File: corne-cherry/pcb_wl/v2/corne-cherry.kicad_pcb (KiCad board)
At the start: 2 copper layers, 152.8 x 91.4 mm, 72 parts, among them J1 MJ-4PP-9, J2 OLED, J3 Conn_01x02_Female, SW1 SW_PUSH, SW10 SW_PUSH, SW11 SW_PUSH, SW12 SW_PUSH, SW13 SW_PUSH, SW14 SW_PUSH, SW15 SW_PUSH, SW16 SW_PUSH, SW17 SW_PUSH, SW18 SW_PUSH, SW19 SW_PUSH, SW2 SW_PUSH, SW20 SW_PUSH, SW21 SW_PUSH, SW22 SW_PUSH, SW23 SW_SPDT, SW24 SW_SPDT, SW3 SW_PUSH, SW4 SW_PUSH, SW5 SW_PUSH, SW6 SW_PUSH, SW7 SW_PUSH, SW8 SW_PUSH, SW9 SW_PUSH, U1 ProMicro

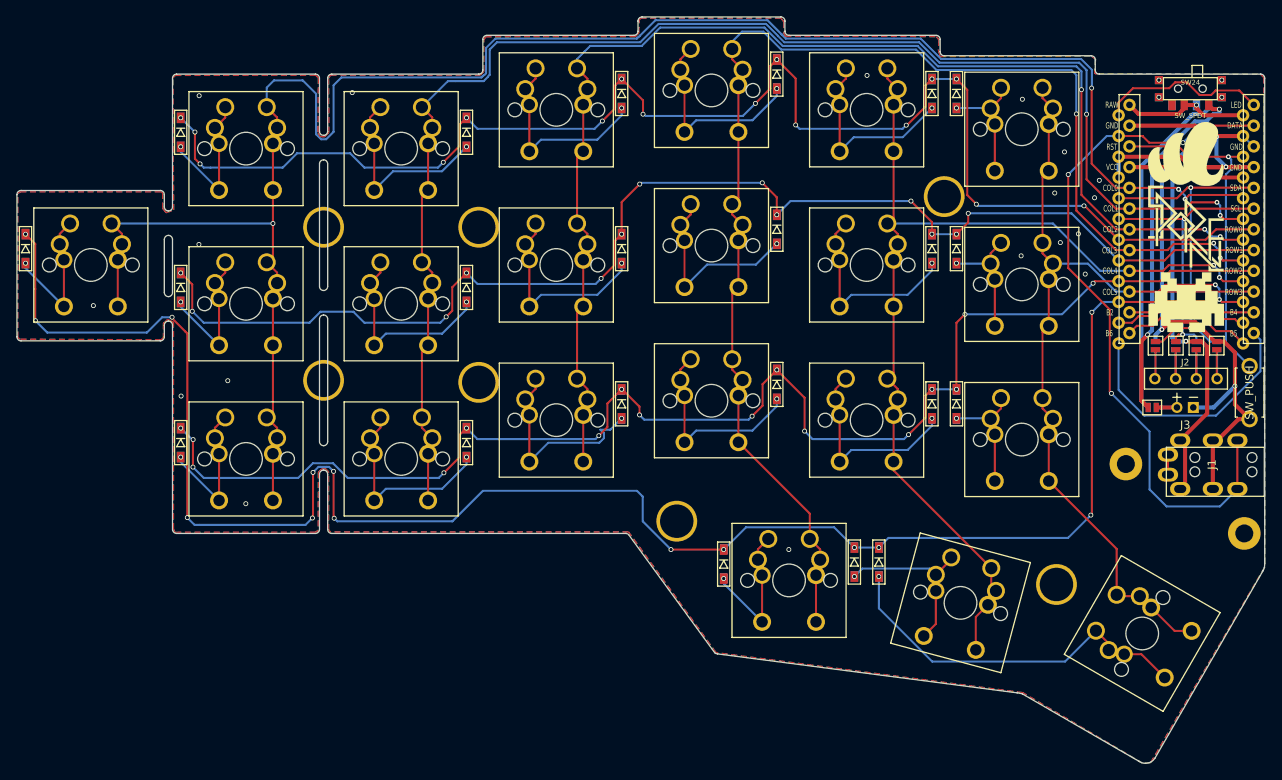
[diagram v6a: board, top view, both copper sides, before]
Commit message: Bigger battery header, cleaner switch footprints and schematic
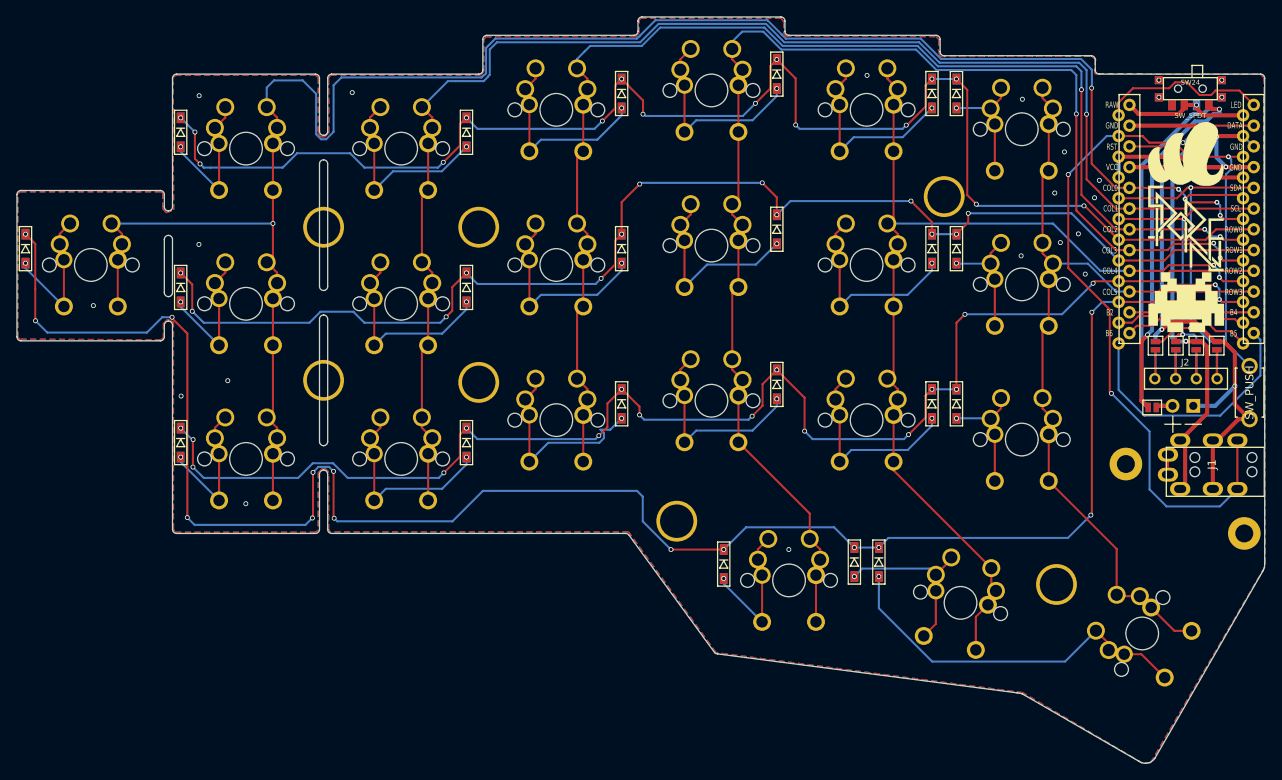
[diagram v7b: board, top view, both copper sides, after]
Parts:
- G1, G2: renamed from G***; value LOGO -> Logo_Open_Hardware_Small
- J3: footprint Connector_PinHeader_2.00mm:PinHeader_1x02_P2.00mm_Vertical -> kbd:Battery_Header
- SW1, SW10, SW11, SW12, SW13, SW14, SW15, SW16, SW17, SW18, SW19, SW2, SW20, SW22, SW3, SW4, SW5, SW6, SW7, SW8, SW9: footprint Button_Switch_Keyboard:MX_Hitek_725_1U_reversible -> kbd:MX_Hitek_725_1U_reversible
- SW21: footprint Button_Switch_Keyboard:MX_Hitek_725_1.5U_reversible -> kbd:MX_Hitek_725_1.5U_reversible
- moved J3 1.01 mm to (186.0, 108.6), turned to 270 degrees
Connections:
- SW23 pad 1: (no net) -> Net-(SW23-Pad1)
- SW24 pad 3: (no net) -> Net-(SW24-Pad3)
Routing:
- net Net-(J3-Pad2): track 5.06 -> 4.13 mm
